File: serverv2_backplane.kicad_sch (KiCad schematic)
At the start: 55 parts, among them CN5 W25Q128FVIQ_Connector, Q6 CSD18513Q5A, Q7 CSD18513Q5A, U10 TPS55288RPMR, U11 220uF, U15 TPS65987DDHRSHR

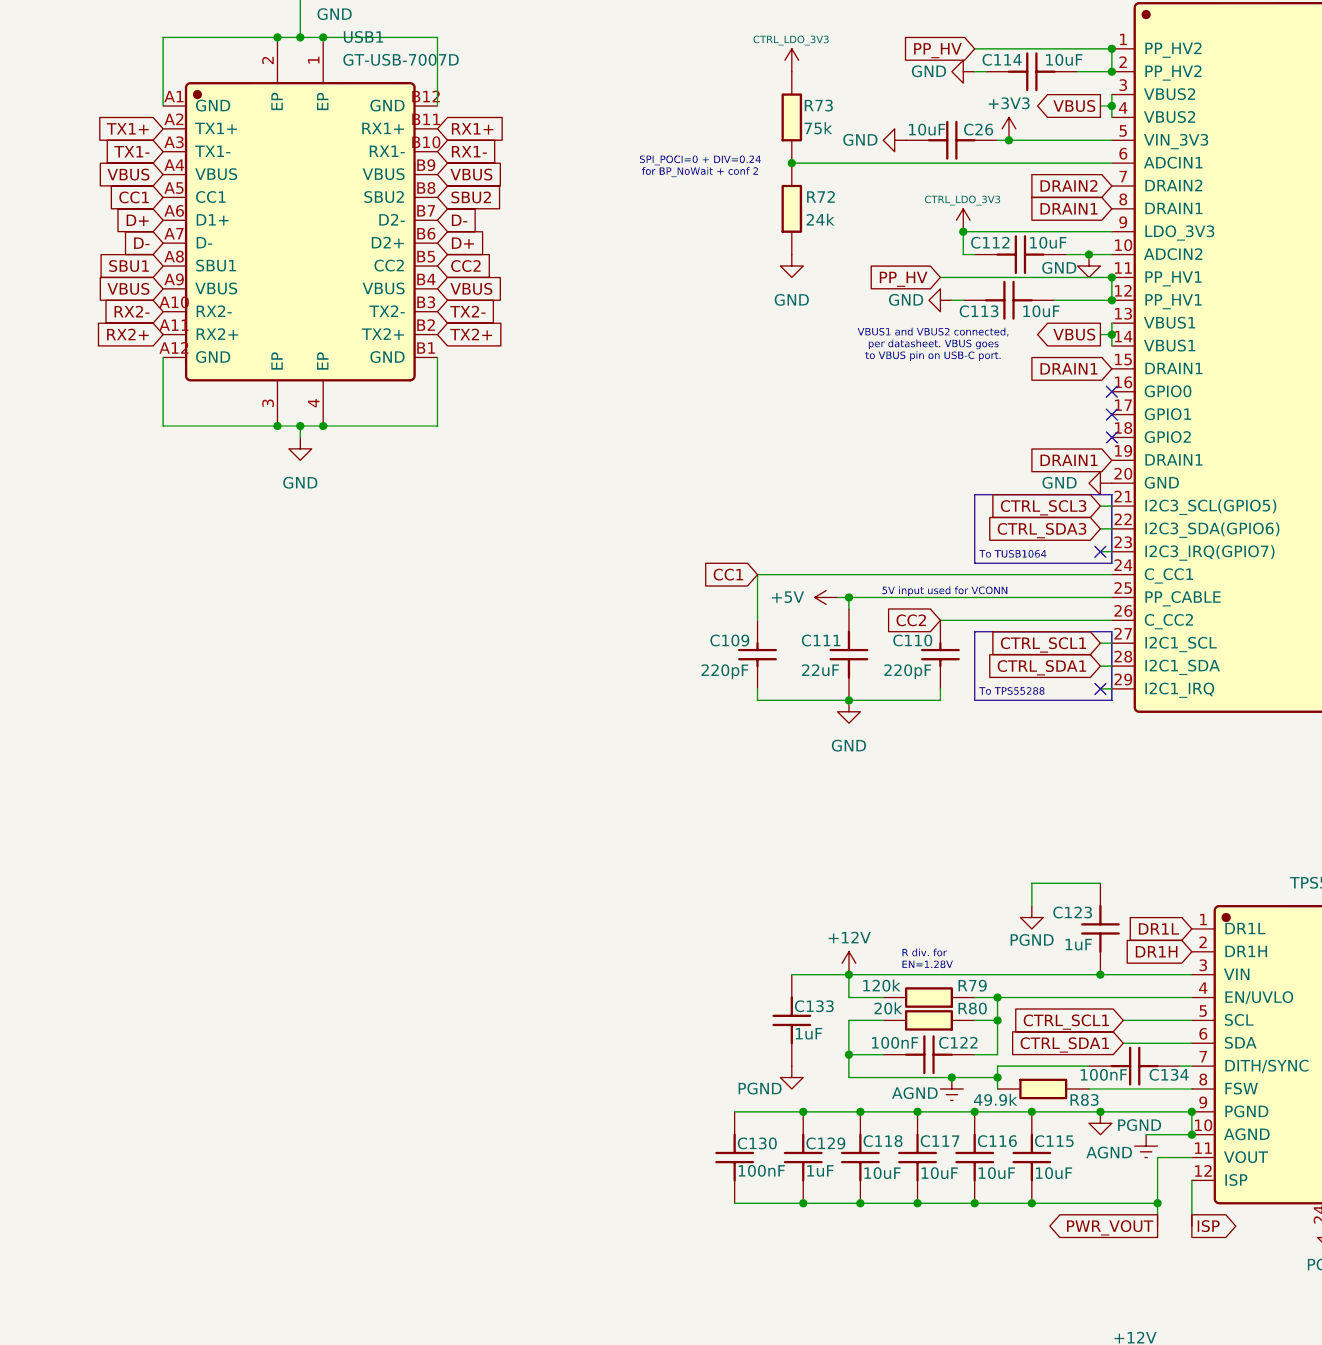
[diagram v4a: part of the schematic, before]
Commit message: Preliminary design of power monitor for PSU rails and USB-C VBUS
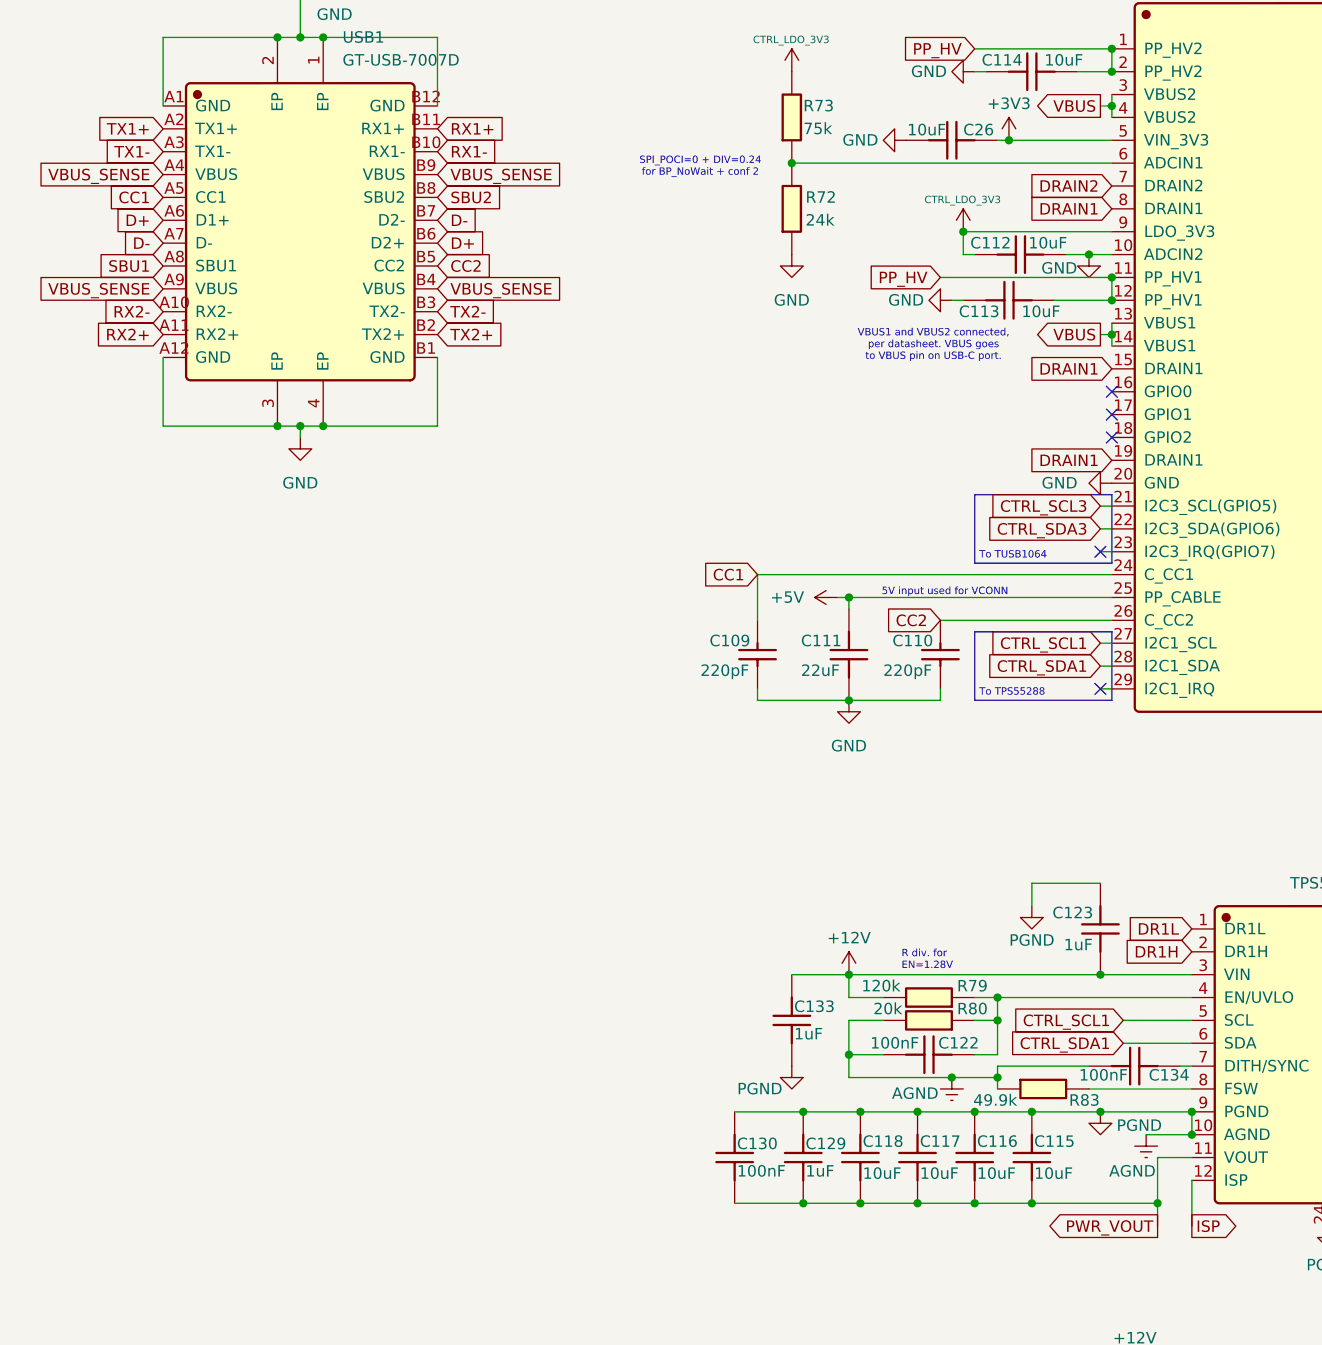
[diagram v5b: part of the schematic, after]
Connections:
- net VBUS: no longer USB1.A4 (VBUS), USB1.A9 (VBUS), USB1.B4 (VBUS), USB1.B9 (VBUS)
- new net VBUS_SENSE: USB1.A4 (VBUS), USB1.A9 (VBUS), USB1.B4 (VBUS), USB1.B9 (VBUS)
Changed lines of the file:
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@@
 	)
 	(junction
-		(at 134.62 59.69)
-		(diameter 0)
-		(color 0 0 0 0)
-	)
-	(junction
 		(at 144.78 180.34)
 		(diameter 0)
@@
 	)
 	(junction
+		(at 134.62 59.69)
+		(diameter 0)
+		(color 0 0 0 0)
+	)
+	(junction
 		(at 143.51 146.05)
 		(diameter 0)
@@
 		)
 	)
+	(global_label "VBUS_SENSE"
+		(shape input)
+		(at 59.69 54.61 0)
+		(fields_autoplaced yes)
+		(effects
+			(font
+				(size 1.27 1.27)
+			)
+			(justify left)
+		)
+		(property "Intersheetrefs" "${INTERSHEET_REFS}"
+			(at 74.5889 54.61 0)
+			(hide yes)
+			(show_name no)
+			(do_not_autoplace no)
+			(effects
+				(font
+					(size 1.27 1.27)
+				)
+				(justify left)
+			)
+		)
+	)
 	(global_label "DRAIN2"
 		(shape input)
@@
 		)
 	)
+	(global_label "VBUS_SENSE"
+		(shape input)
+		(at 59.69 41.91 0)
+		(fields_autoplaced yes)
+		(effects
+			(font
+				(size 1.27 1.27)
+			)
+			(justify left)
+		)
+		(property "Intersheetrefs" "${INTERSHEET_REFS}"
+			(at 74.5889 41.91 0)
+			(hide yes)
+			(show_name no)
+			(do_not_autoplace no)
+			(effects
+				(font
+					(size 1.27 1.27)
+				)
+				(justify left)
+			)
+		)
+	)
 	(global_label "TX2+"
 		(shape input)
@@
 		)
 	)
-	(global_label "VBUS"
-		(shape input)
-		(at 59.69 54.61 0)
-		(fields_autoplaced yes)
-		(effects
-			(font
-				(size 1.27 1.27)
-			)
-			(justify left)
-		)
-		(property "Intersheetrefs" "${INTERSHEET_REFS}"
-			(at 67.5738 54.61 0)
-			(hide yes)
-			(show_name no)
-			(do_not_autoplace no)
-			(effects
-				(font
-					(size 1.27 1.27)
-				)
-				(justify left)
-			)
-		)
-	)
 	(global_label "TX1-"
 		(shape input)
@@
 		)
 	)
-	(global_label "VBUS"
+	(global_label "ISN"
 		(shape input)
-		(at 29.21 41.91 180)
+		(at 251.46 142.24 180)
 		(fields_autoplaced yes)
 		(effects
@@
 		)
 		(property "Intersheetrefs" "${INTERSHEET_REFS}"
-			(at 21.3262 41.91 0)
+			(at 245.33 142.24 0)
 			(hide yes)
 			(show_name no)
@@
 		)
 	)
-	(global_label "ISN"
+	(global_label "VBUS_SENSE"
 		(shape input)
-		(at 251.46 142.24 180)
+		(at 29.21 41.91 180)
 		(fields_autoplaced yes)
 		(effects
@@
 		)
 		(property "Intersheetrefs" "${INTERSHEET_REFS}"
-			(at 245.33 142.24 0)
+			(at 14.3111 41.91 0)
 			(hide yes)
 			(show_name no)
@@
 		)
 	)
-	(global_label "VBUS"
+	(global_label "VBUS_SENSE"
 		(shape input)
 		(at 29.21 54.61 180)
@@
 		)
 		(property "Intersheetrefs" "${INTERSHEET_REFS}"
-			(at 21.3262 54.61 0)
+			(at 14.3111 54.61 0)
 			(hide yes)
 			(show_name no)
@@
 		)
 	)
-	(global_label "VBUS"
-		(shape input)
-		(at 59.69 41.91 0)
-		(fields_autoplaced yes)
-		(effects
-			(font
-				(size 1.27 1.27)
-			)
-			(justify left)
-		)
-		(property "Intersheetrefs" "${INTERSHEET_REFS}"
-			(at 67.5738 41.91 0)
-			(hide yes)
-			(show_name no)
-			(do_not_autoplace no)
-			(effects
-				(font
-					(size 1.27 1.27)
-				)
-				(justify left)
-			)
-		)
-	)
 	(global_label "PWR_FAULT"
 		(shape input)
@@
 		)
 		(property "Value" "AGND"
-			(at 134.366 150.622 0)
+			(at 136.906 152.654 0)
 			(show_name no)
 			(do_not_autoplace no)

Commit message: Mostly complete initial transfer to hierarchical schematic
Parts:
- removed C109, C110: 220pF, Capacitor_SMD:C_0402_1005Metric, symbol JLCImport:0402B221K500NT
- removed C111: 22uF, Capacitor_SMD:C_0603_1608Metric, symbol JLCImport:CL10A226MQ8NRNC
- removed C112, C26: 10uF, Capacitor_SMD:C_0603_1608Metric, symbol JLCImport:CL10A106KP8NNNC
- removed C113, C114, C115, C116, C117, C118, C125, C126: 10uF, Capacitor_SMD:C_0805_2012Metric, symbol JLCImport:CL21A106KAYNNNE
- removed C119, C120, C122, C124, C130, C134: 100nF, Capacitor_SMD:C_0402_1005Metric, symbol JLCImport:CL05B104KB54PNC
- removed C121: 4.7uF, Capacitor_SMD:C_0805_2012Metric, symbol JLCImport:CL21A475KAQNNNE
- removed C123: 1uF, Capacitor_SMD:C_0603_1608Metric, symbol JLCImport:CL10A105KB8NNNC
- removed C127: 100pF, Capacitor_SMD:C_0402_1005Metric, symbol JLCImport:TCC0402COG101J101AT
- removed C128: 4.7nF, Capacitor_SMD:C_0402_1005Metric, symbol JLCImport:CGA0402X7R472K250GT
- removed C129, C132, C133: 1uF, Capacitor_SMD:C_0402_1005Metric, symbol JLCImport:CL05A105KA5NQNC
- removed C131: 68uF, JLCImport:DHG100M686G150S1AA, symbol JLCImport:DHG100M686G150S1AA
- removed CN5: W25Q128FVIQ_Connector, JLCImport:H2541FV-C762-2X04P, symbol JLCImport:H2541FV-C762-2X04P
- removed L12: 4.7uH, JLCImport:SL1040-4R7M, symbol JLCImport:SL1040-4R7M
- removed Q6, Q7: CSD18513Q5A, JLCImport:CSD18513Q5A, symbol JLCImport:CSD18513Q5A
- removed R72: 24k, Resistor_SMD:R_0603_1608Metric, symbol JLCImport:0603WAF2402T5E
- removed R73: 75k, Resistor_SMD:R_0603_1608Metric, symbol JLCImport:0603WAF7502T5E
- removed R74: 0, Resistor_SMD:R_0402_1005Metric, symbol JLCImport:0402WGF0000TCE
- removed R75, R76, R77, R78: 3.3k, Resistor_SMD:R_0402_1005Metric, symbol JLCImport:0402WGF3301TCE
- removed R79: 120k, Resistor_SMD:R_0603_1608Metric, symbol JLCImport:0603WAF1203T5E
- removed R80: 20k, Resistor_SMD:R_0402_1005Metric, symbol JLCImport:0402WGF2002TCE
- removed R81, R82: 1.0, Resistor_SMD:R_0402_1005Metric, symbol JLCImport:WR04W1R00FTL
- removed R83: 49.9k, Resistor_SMD:R_0402_1005Metric, symbol JLCImport:RMS04FT4992
- removed R84: 6.2k, Resistor_SMD:R_0603_1608Metric, symbol JLCImport:0603WAF6201T5E
- removed R85: 10k, Resistor_SMD:R_0402_1005Metric, symbol JLCImport:0402WGF1002TCE
- removed R86: 10mΩ, Resistor_SMD:R_1206_3216Metric, symbol JLCImport:1206W3J010LT5E
- removed R87, R88: 10.0, Resistor_SMD:R_0402_1005Metric, symbol JLCImport:0402WGF100JTCE
- removed R89: 56.2k, Resistor_SMD:R_0402_1005Metric, symbol JLCImport:0402WGF5622TCE
- removed R90: 42.2k, Resistor_SMD:R_0402_1005Metric, symbol JLCImport:CR0402F42K2Q10Z
- removed R91: 150k, Resistor_SMD:R_0603_1608Metric, symbol JLCImport:0603WAF1503T5E
- removed U10: TPS55288RPMR, JLCImport:TPS55288RPMR, symbol JLCImport:TPS55288RPMR
- removed U11: 220uF, TerminalBlock_Phoenix:TerminalBlock_Phoenix_PTSM-0,5-2-2.5-V-THR_1x02_P2.50mm_Vertical, symbol JLCImport:CD110227M1E0612VFL
- removed U15: TPS65987DDHRSHR, Package_DFN_QFN:VQFN-40-1EP_5x5mm_P0.4mm_EP3.3x3.3mm, symbol JLCImport:TPS65987DDHRSHR
- removed USB1: GT-USB-7007D, Connector_USB:USB_C_Receptacle_G-Switch_GT-USB-7025, symbol JLCImport:GT-USB-7007D
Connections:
- no-connect marks 16 -> 0
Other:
- added sheet DISP_HEADER (DISP_HEADER.kicad_sch)
- added sheet FAN_HEADER_0 (FAN_HEADER.kicad_sch)
- added sheet FAN_HEADER_1 (FAN_HEADER.kicad_sch)
- added sheet FAN_HEADER_2 (FAN_HEADER.kicad_sch)
- added sheet FAN_HEADER_3 (FAN_HEADER.kicad_sch)
- added sheet FPC_CONN (FPC_CONN.kicad_sch)
- added sheet M.2_0 (M.2_0.kicad_sch)
- added sheet M.2_1 (M.2_0.kicad_sch)
- added sheet MCP9808 (MCP9808.kicad_sch)
- added sheet PAC1954_FANS (PAC1954_FANS.kicad_sch)
- added sheet PAC1954_HUB (PAC1954_HUB.kicad_sch)
- added sheet PAC1954_PSU_PD (PAC1954_PSU_PD.kicad_sch)
- added sheet PANEL_HEADER (PANEL_HEADER.kicad_sch)
- added sheet PORT5_USB (PORT5_USB.kicad_sch)
- added sheet PORT6_USB (PORT6_USB.kicad_sch)
- added sheet PS176 (PS176.kicad_sch)
- added sheet PSU_CONN (PSU_CONN.kicad_sch)
- added sheet RTL9210B_0 (RTL9210B_0.kicad_sch)
- added sheet RTL9210B_1 (RTL9210B_0.kicad_sch)
- added sheet SATA_SUBSYSTEM_0 (SATA_SUBSYSTEM.kicad_sch)
- added sheet SD_SLOT (SD_SLOT.kicad_sch)
- added sheet SG2002_HEADER (SG2002_HEADER.kicad_sch)
- added sheet TC358743 (TC358743.kicad_sch)
- added sheet TPS55288 (TPS55288.kicad_sch)
- added sheet TPS65987D (TPS65987D.kicad_sch)
- added sheet TUSB1064 (TUSB1064.kicad_sch)
- added sheet UCS2113 (UCS2113.kicad_sch)
- added sheet USB2244i (USB2244i.kicad_sch)
- added sheet USB7206C (USB7206C.kicad_sch)
- added sheet Upstream_USB-C (upstream_usb-c.kicad_sch)
- note removed: "5V input used for VCONN"
- note removed: "6.2k b/w MODE and GND to set I2C addr, per EVM"
- note removed: "BC1.2 not used so leave C_USB floating - verify this"
- note removed: "Connect FB/INT to GPIO on MCU to track fault indicator"
- note removed: "DP_HPD connected to TUSB1064 and PS176"
- note removed: "R div. for EN=1.28V"
- note removed: "SPI_POCI=0 + DIV=0.24 for BP_NoWait + conf 2"
- note removed: "This inductor does not meet the recommended DCR spec; hopefully it still works!!"
- note removed: "To RP2350B"
- note removed: "To TPS55288"
- note removed: "To TUSB1064"
- note removed: "VBUS1 and VBUS2 connected, per datasheet. VBUS goes to VBUS pin on USB-C port."

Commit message: Transferred everything to hierarchical schematic and wired PSU power on circuit AND created duplicate schematics for all relevant subsystems
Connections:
- no-connect marks 0 -> 15
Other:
- added sheet PAC1954_IPKVM_DISP (PAC1954_IPKVM_DISP.kicad_sch)
- added sheet PWR_BTN (PWR_BTN.kicad_sch)
- added sheet RP2350B_0 (RP2350B_0.kicad_sch)
- added sheet RP2350B_1 (RP2350B_0.kicad_sch)
- added sheet RP2350B_2 (RP2350B_0.kicad_sch)
- added sheet SATA_SUBSYSTEM_1 (SATA_SUBSYSTEM.kicad_sch)
- added sheet SATA_SUBSYSTEM_10 (SATA_SUBSYSTEM.kicad_sch)
- added sheet SATA_SUBSYSTEM_11 (SATA_SUBSYSTEM.kicad_sch)
- added sheet SATA_SUBSYSTEM_2 (SATA_SUBSYSTEM.kicad_sch)
- added sheet SATA_SUBSYSTEM_3 (SATA_SUBSYSTEM.kicad_sch)
- added sheet SATA_SUBSYSTEM_4 (SATA_SUBSYSTEM.kicad_sch)
- added sheet SATA_SUBSYSTEM_5 (SATA_SUBSYSTEM.kicad_sch)
- added sheet SATA_SUBSYSTEM_6 (SATA_SUBSYSTEM.kicad_sch)
- added sheet SATA_SUBSYSTEM_7 (SATA_SUBSYSTEM.kicad_sch)
- added sheet SATA_SUBSYSTEM_8 (SATA_SUBSYSTEM.kicad_sch)
- added sheet SATA_SUBSYSTEM_9 (SATA_SUBSYSTEM.kicad_sch)
- sheet PSU_CONN ports: added +3V3SB; removed none
- sheet SG2002_HEADER ports: added A_OSCK, A_SCK, A_SD, A_WFS, DISP_BL, DISP_CS, DISP_DC, DISP_MOSI, DISP_RST, DISP_SCLK, SCL1, SCL3, SDA1, SDA3, TOUCH_INT, TOUCH_RST; removed +3V3
- sheet TC358743 ports: added +3V3_CSI; removed none
- note added: "FAN_PWM_0"
- note added: "FAN_PWM_1"
- note added: "FAN_PWM_2"
- note added: "FAN_PWM_3"
- note added: "FAN_TACH_0"
- note added: "FAN_TACH_1"
- note added: "FAN_TACH_2"
- note added: "FAN_TACH_3"
- note added: "PSU_ON#"
- note added: "PWR_OK"
- note added: "RP2350B_0 is tied to +3V3SB to handle PSU power sequencing"
- note added: "SATA_12V_EN#_0"
- note added: "SATA_12V_EN#_1"
- note added: "SATA_12V_EN#_10"
- note added: "SATA_12V_EN#_11"
- note added: "SATA_12V_EN#_2"
- note added: "SATA_12V_EN#_3"
- note added: "SATA_12V_EN#_4"
- note added: "SATA_12V_EN#_5"
- note added: "SATA_12V_EN#_6"
- note added: "SATA_12V_EN#_7"
- note added: "SATA_12V_EN#_8"
- note added: "SATA_12V_EN#_9"
- note added: "SATA_12V_FLT_0"
- note added: "SATA_12V_FLT_1"
- note added: "SATA_12V_FLT_10"
- note added: "SATA_12V_FLT_11"
- note added: "SATA_12V_FLT_2"
- note added: "SATA_12V_FLT_3"
- note added: "SATA_12V_FLT_4"
- note added: "SATA_12V_FLT_5"
- note added: "SATA_12V_FLT_6"
- note added: "SATA_12V_FLT_7"
- note added: "SATA_12V_FLT_8"
- note added: "SATA_12V_FLT_9"
- note added: "SATA_12V_I_SENSE_0"
- note added: "SATA_12V_I_SENSE_1"
- note added: "SATA_12V_I_SENSE_10"
- note added: "SATA_12V_I_SENSE_11"
- note added: "SATA_12V_I_SENSE_2"
- note added: "SATA_12V_I_SENSE_3"
- note added: "SATA_12V_I_SENSE_4"
- note added: "SATA_12V_I_SENSE_5"
- note added: "SATA_12V_I_SENSE_6"
- note added: "SATA_12V_I_SENSE_7"
- note added: "SATA_12V_I_SENSE_8"
- note added: "SATA_12V_I_SENSE_9"
- note added: "SATA_5V_EN#_0"
- note added: "SATA_5V_EN#_1"
- note added: "SATA_5V_EN#_10"
- note added: "SATA_5V_EN#_11"
- note added: "SATA_5V_EN#_2"
- note added: "SATA_5V_EN#_3"
- note added: "SATA_5V_EN#_4"
- note added: "SATA_5V_EN#_5"
- note added: "SATA_5V_EN#_6"
- note added: "SATA_5V_EN#_7"
- note added: "SATA_5V_EN#_8"
- note added: "SATA_5V_EN#_9"
- note added: "SATA_5V_FLT_0"
- note added: "SATA_5V_FLT_1"
- note added: "SATA_5V_FLT_10"
- note added: "SATA_5V_FLT_11"
- note added: "SATA_5V_FLT_2"
- note added: "SATA_5V_FLT_3"
- note added: "SATA_5V_FLT_4"
- note added: "SATA_5V_FLT_5"
- note added: "SATA_5V_FLT_6"
- note added: "SATA_5V_FLT_7"
- note added: "SATA_5V_FLT_8"
- note added: "SATA_5V_FLT_9"
- note added: "SATA_5V_I_SENSE_0"
- note added: "SATA_5V_I_SENSE_1"
- note added: "SATA_5V_I_SENSE_10"
- note added: "SATA_5V_I_SENSE_11"
- note added: "SATA_5V_I_SENSE_2"
- note added: "SATA_5V_I_SENSE_3"
- note added: "SATA_5V_I_SENSE_4"
- note added: "SATA_5V_I_SENSE_5"
- note added: "SATA_5V_I_SENSE_6"
- note added: "SATA_5V_I_SENSE_7"
- note added: "SATA_5V_I_SENSE_8"
- note added: "SATA_5V_I_SENSE_9"
- note added: "SATA_DSS_CTRL_0"
- note added: "SATA_DSS_CTRL_1"
- note added: "SATA_DSS_CTRL_10"
- note added: "SATA_DSS_CTRL_11"
- note added: "SATA_DSS_CTRL_2"
- note added: "SATA_DSS_CTRL_4"
- note added: "SATA_DSS_CTRL_5"
- note added: "SATA_DSS_CTRL_6"
- note added: "SATA_DSS_CTRL_7"
- note added: "SATA_DSS_CTRL_8"
- note added: "SATA_DSS_CTRL_9"

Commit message: Cleaned up schematic and replaced TC358743XBG with reverse-engineered LT6911C
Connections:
- no-connect marks 15 -> 16
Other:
- removed sheet TC358743
- added sheet LT6911UXC (LT6911UXC.kicad_sch)
- sheet FPC_CONN ports: added INT; removed none
- note added: "Audio output disabled due to Sipeed's LT6911C implementation not including audio pin connections."
